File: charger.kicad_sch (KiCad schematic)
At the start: 39 parts, among them Q1 NMOS, Q2 NMOS, Q3 NMOS, SW3 SW_SPST, U2 BQ25798RQMR

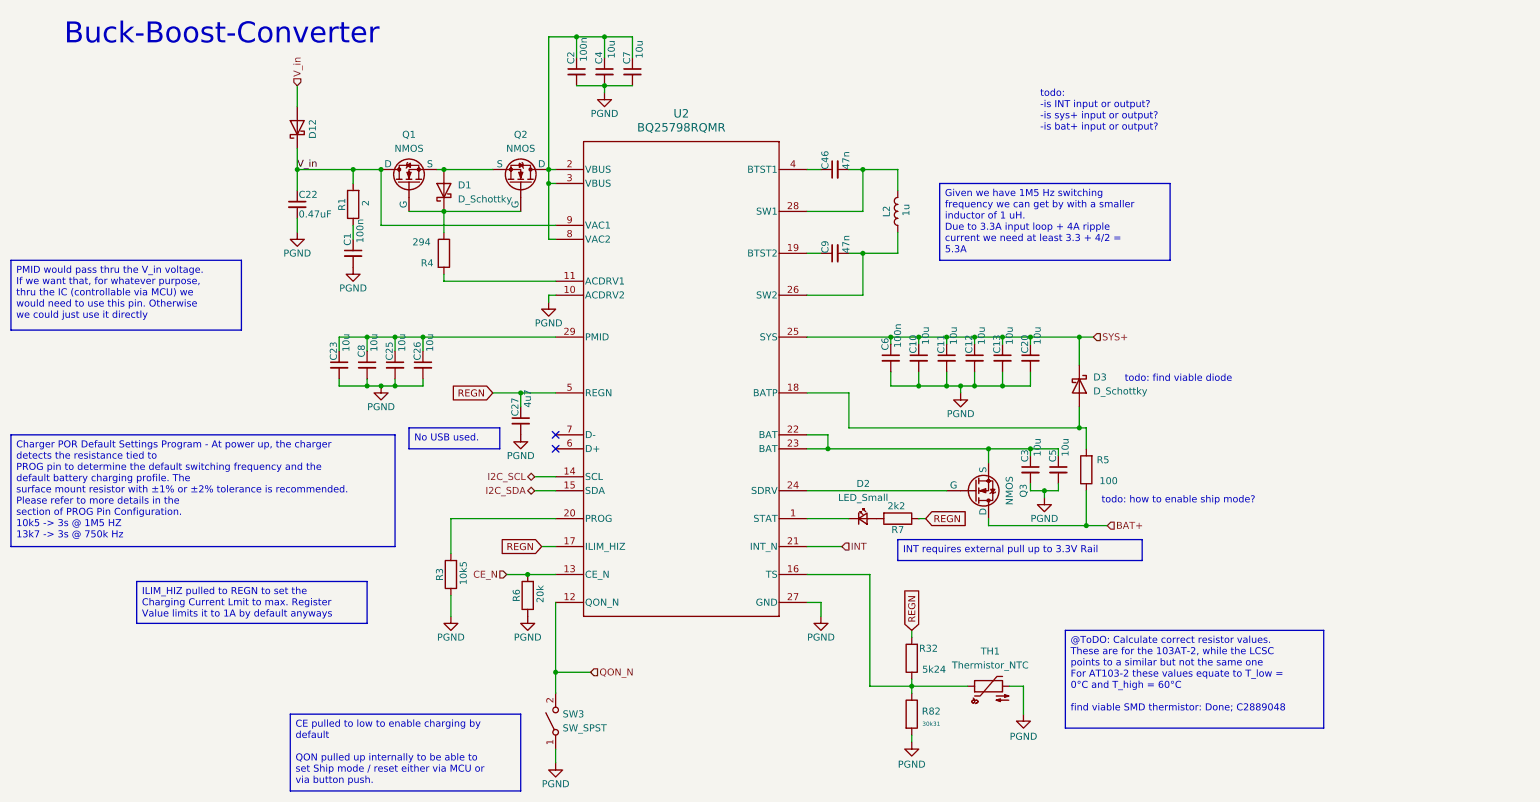
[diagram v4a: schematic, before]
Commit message: cleaned up hierarchical structure; changed connectors
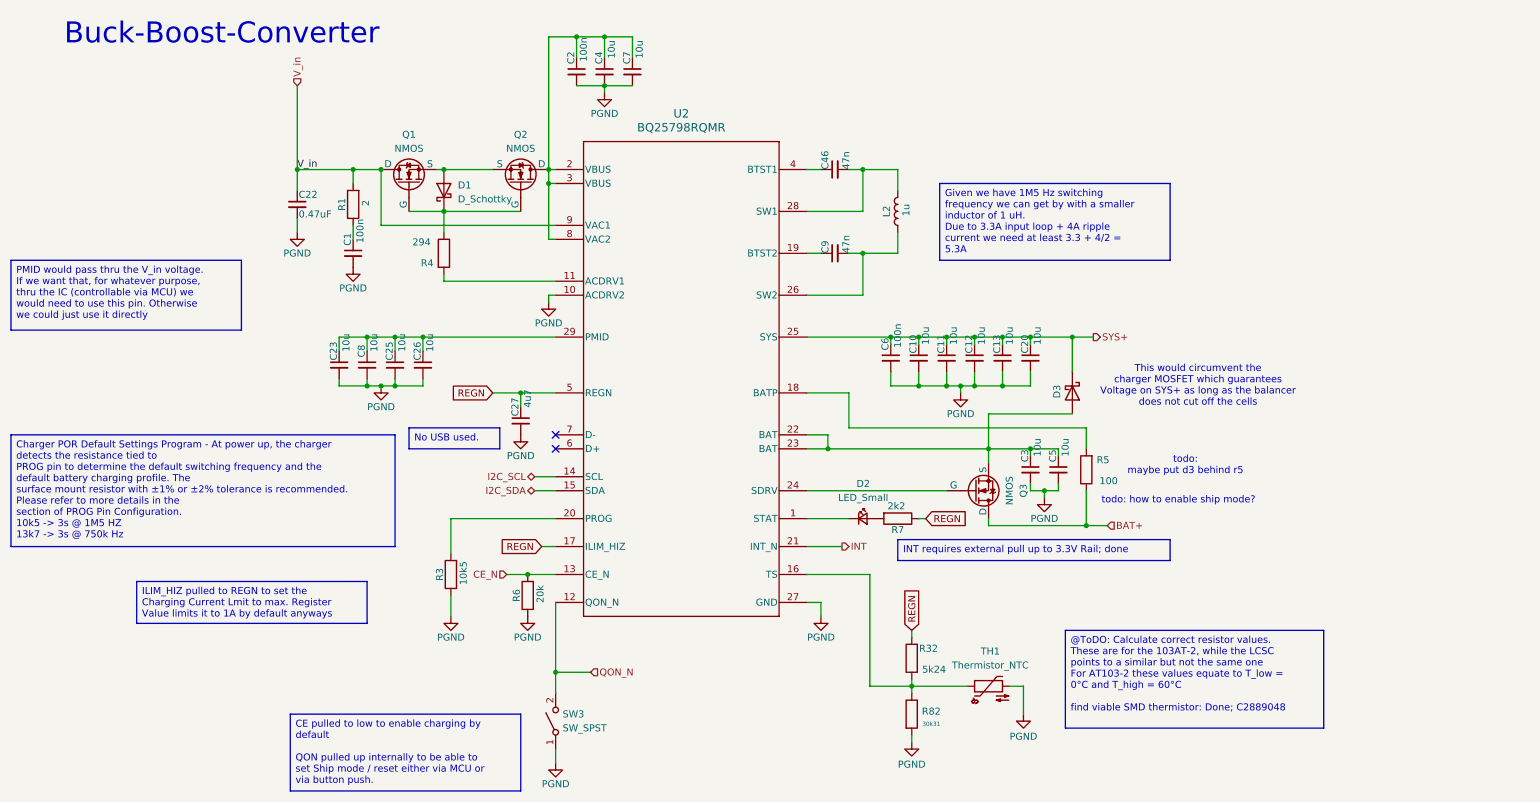
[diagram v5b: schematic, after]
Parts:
- removed D12: ~, Diode_SMD:D_SMA, symbol Device:D_Schottky
- D3: value D_Schottky -> ~; footprint (none) -> Diode_SMD:D_SMA; LCSC (none) -> C3011043
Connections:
- net at R5.2, U2.18 (BATP): no longer D3.2 (A)
- net at C3.1, C5.1, Q3.3 (S)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: now also D3.2 (A)
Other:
- note added: "This would circumvent the charger MOSFET which guarantees Voltage on SYS+ as long as the balancer does not cut off the cells"
- note added: "todo: maybe put d3 behind r5"
- note removed: "todo: -is INT input or output? -is sys+ input or output? -is bat+ input or output?"
- note removed: "todo: find viable diode"
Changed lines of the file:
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@@
 		)
 	)
-	(text "todo: \n-is INT input or output?\n-is sys+ input or output?\n-is bat+ input or output?"
+	(text "todo: \nmaybe put d3 behind r5"
 		(exclude_from_sim no)
-		(at 201.168 31.242 0)
+		(at 227.584 95.758 0)
 		(effects
 			(font
 				(size 1.27 1.27)
 			)
-			(justify left)
 		)
 	)
-	(text "todo: find viable diode"
+	(text "This would circumvent the \ncharger MOSFET which guarantees\nVoltage on SYS+ as long as the balancer \ndoes not cut off the cells"
 		(exclude_from_sim no)
-		(at 226.314 80.01 0)
+		(at 229.87 81.28 0)
 		(effects
 			(font
@@
 		)
 	)
-	(text_box "INT requires external pull up to 3.3V Rail"
+	(text_box "INT requires external pull up to 3.3V Rail; done"
 		(exclude_from_sim no)
 		(at 175.26 109.22 0)
-		(size 44.45 3.81)
+		(size 49.53 3.81)
 		(margins 0.9525 0.9525 0.9525 0.9525)
 		(stroke
@@
 	)
 	(junction
-		(at 208.28 72.39)
-		(diameter 0)
-		(color 0 0 0 0)
-	)
-	(junction
 		(at 111.76 41.91)
 		(diameter 0)
@@
 	)
 	(junction
-		(at 208.28 88.9)
-		(diameter 0)
-		(color 0 0 0 0)
-	)
-	(junction
 		(at 168.91 41.91)
 		(diameter 0)
@@
 	)
 	(junction
+		(at 207.01 72.39)
+		(diameter 0)
+		(color 0 0 0 0)
+	)
+	(junction
 		(at 199.39 72.39)
 		(diameter 0)
@@
 	(wire
 		(pts
-			(xy 208.28 72.39) (xy 208.28 77.47)
-		)
-		(stroke
-			(width 0)
-			(type default)
-		)
-	)
-	(wire
-		(pts
 			(xy 204.47 100.33) (xy 201.93 100.33)
 		)
@@
 	(wire
 		(pts
-			(xy 166.37 88.9) (xy 208.28 88.9)
-		)
-		(stroke
-			(width 0)
-			(type default)
-		)
-	)
-	(wire
-		(pts
 			(xy 66.04 41.91) (xy 66.04 45.72)
 		)
@@
 	(wire
 		(pts
-			(xy 66.04 50.8) (xy 66.04 53.34)
+			(xy 191.77 86.36) (xy 191.77 92.71)
 		)
 		(stroke
@@
 	(wire
 		(pts
-			(xy 158.75 41.91) (xy 161.29 41.91)
+			(xy 66.04 50.8) (xy 66.04 53.34)
 		)
 		(stroke
@@
 	(wire
 		(pts
-			(xy 175.26 57.15) (xy 168.91 57.15)
+			(xy 158.75 41.91) (xy 161.29 41.91)
 		)
 		(stroke
@@
 	(wire
 		(pts
-			(xy 113.03 54.61) (xy 111.76 54.61)
+			(xy 175.26 57.15) (xy 168.91 57.15)
 		)
 		(stroke
@@
 	(wire
 		(pts
-			(xy 66.04 26.67) (xy 66.04 30.48)
+			(xy 113.03 54.61) (xy 111.76 54.61)
 		)
 		(stroke
@@
 	(wire
 		(pts
-			(xy 208.28 88.9) (xy 209.55 88.9)
+			(xy 166.37 88.9) (xy 209.55 88.9)
 		)
 		(stroke
@@
 	(wire
 		(pts
-			(xy 208.28 72.39) (xy 199.39 72.39)
+			(xy 199.39 72.39) (xy 207.01 72.39)
 		)
 		(stroke
@@
 	(wire
 		(pts
+			(xy 207.01 72.39) (xy 207.01 78.74)
+		)
+		(stroke
+			(width 0)
+			(type default)
+		)
+	)
+	(wire
+		(pts
 			(xy 88.9 81.28) (xy 83.82 81.28)
 		)
@@
 	(wire
 		(pts
-			(xy 66.04 38.1) (xy 66.04 41.91)
+			(xy 66.04 26.67) (xy 66.04 41.91)
 		)
 		(stroke
@@
 	(wire
 		(pts
+			(xy 207.01 72.39) (xy 210.82 72.39)
+		)
+		(stroke
+			(width 0)
+			(type default)
+		)
+	)
+	(wire
+		(pts
 			(xy 184.15 73.66) (xy 184.15 72.39)
 		)
@@
 	(wire
 		(pts
+			(xy 191.77 86.36) (xy 207.01 86.36)
+		)
+		(stroke
+			(width 0)
+			(type default)
+		)
+	)
+	(wire
+		(pts
 			(xy 162.56 92.71) (xy 191.77 92.71)
 		)
@@
 	(wire
 		(pts
-			(xy 208.28 85.09) (xy 208.28 88.9)
-		)
-		(stroke
-			(width 0)
-			(type default)
-		)
-	)
-	(wire
-		(pts
 			(xy 168.91 41.91) (xy 175.26 41.91)
 		)
@@
 	(wire
 		(pts
-			(xy 210.82 72.39) (xy 208.28 72.39)
-		)
-		(stroke
-			(width 0)
-			(type default)
-		)
-	)
-	(wire
-		(pts
 			(xy 88.9 80.01) (xy 88.9 81.28)
 		)
@@
 	)
 	(hierarchical_label "INT"
-		(shape input)
+		(shape output)
 		(at 165.1 110.49 0)
 		(effects
@@
 	)
 	(hierarchical_label "SYS+"
-		(shape input)
+		(shape output)
 		(at 210.82 72.39 0)
 		(effects
@@
 	)
 	(symbol
-		(lib_id "Device:D_Schottky")
-		(at 208.28 81.28 270)
-		(unit 1)
-		(exclude_from_sim no)
-		(in_bom yes)
-		(on_board yes)
-		(dnp no)
-		(fields_autoplaced yes)
-		(property "Reference" "D3"
-			(at 210.82 79.6924 90)
-			(effects
-				(font
-					(size 1.27 1.27)
-				)
-				(justify left)
-			)
-		)
-		(property "Value" "D_Schottky"
-			(at 210.82 82.2324 90)
-			(effects
-				(font
-					(size 1.27 1.27)
-				)
-				(justify left)
-			)
-		)
-		(property "Footprint" ""
-			(at 208.28 81.28 0)
-			(effects
-				(font
-					(size 1.27 1.27)
-				)
-				(hide yes)
-			)
-		)
-		(property "Datasheet" "~"
-			(at 208.28 81.28 0)
-			(effects
-				(font
-					(size 1.27 1.27)
-				)
-				(hide yes)
-			)
-		)
-		(property "Description" "Schottky diode"
-			(at 208.28 81.28 0)
-			(effects
-				(font
-					(size 1.27 1.27)
-				)
-				(hide yes)
-			)
-		)
-		(pin "1"
-		)
-		(pin "2"
-		)
-		(instances
-			(project ""
-				(path "/afc8cbd3-9ea8-40a2-afae-ed6bd0fe7e6e/29a18ff5-2f4c-44c0-998a-9c2a7b324824"
-					(reference "D3")
-					(unit 1)
-				)
-			)
-		)
-	)
-	(symbol
 		(lib_id "Device:R")
 		(at 92.71 57.15 0)
@@
 	)
 	(symbol
-		(lib_id "Device:D_Schottky")
-		(at 66.04 34.29 90)
+		(lib_id "power:GND1")
+		(at 201.93 101.6 0)
 		(unit 1)
 		(exclude_from_sim no)
@@
 		(on_board yes)
 		(dnp no)
-		(property "Reference" "D12"
-			(at 68.834 34.544 0)
-			(effects
-				(font
-					(size 1.27 1.27)
-				)
-			)
-		)
-		(property "Value" "~"
-			(at 69.85 34.6075 0)
+		(property "Reference" "#PWR011"
+			(at 201.93 107.95 0)
 			(effects
 				(font
@@
 			)
 		)
-		(property "Footprint" "Diode_SMD:D_SMA"
-			(at 66.04 34.29 0)
+		(property "Value" "PGND"
+			(at 201.93 105.41 0)
 			(effects
 				(font
 					(size 1.27 1.27)
 				)
-				(hide yes)
 			)
 		)
-		(property "Datasheet" "https://www.lcsc.com/datasheet/C22452.pdf"
-			(at 66.04 34.29 0)
+		(property "Footprint" ""
+			(at 201.93 101.6 0)
 			(effects
 				(font
@@
 			)
 		)
-		(property "Description" "Schottky diode"
-			(at 66.04 34.29 0)
+		(property "Datasheet" ""
+			(at 201.93 101.6 0)
 			(effects
 				(font
@@
 			)
 		)
-		(property "LCSC" "C22452"
-			(at 66.04 34.29 0)
+		(property "Description" "Power symbol creates a global label with name \"GND1\" , ground"
+			(at 201.93 101.6 0)
 			(effects
 				(font
@@
 			)
 		)
-		(pin "2"
-		)
 		(pin "1"
 		)
@@
 			(project "rapid_power_module"
 				(path "/afc8cbd3-9ea8-40a2-afae-ed6bd0fe7e6e/29a18ff5-2f4c-44c0-998a-9c2a7b324824"
-					(reference "D12")
+					(reference "#PWR011")
 					(unit 1)
 				)
@@
 	)
 	(symbol
-		(lib_id "power:GND1")
-		(at 201.93 101.6 0)
+		(lib_id "Device:D_Schottky")
+		(at 207.01 82.55 270)
 		(unit 1)
 		(exclude_from_sim no)
@@
 		(on_board yes)
 		(dnp no)
-		(property "Reference" "#PWR011"
-			(at 201.93 107.95 0)
+		(property "Reference" "D3"
+			(at 204.216 82.296 0)
+			(effects
+				(font
+					(size 1.27 1.27)
+				)
+			)
+		)
+		(property "Value" "~"
+			(at 203.2 82.2325 0)
 			(effects
 				(font
@@
 			)
 		)
-		(property "Value" "PGND"
-			(at 201.93 105.41 0)
+		(property "Footprint" "Diode_SMD:D_SMA"
+			(at 207.01 82.55 0)
 			(effects
 				(font
 					(size 1.27 1.27)
 				)
+				(hide yes)
 			)
 		)
-		(property "Footprint" ""
-			(at 201.93 101.6 0)
+		(property "Datasheet" "https://www.lcsc.com/datasheet/C22452.pdf"
+			(at 207.01 82.55 0)
 			(effects
 				(font
@@
 			)
 		)
-		(property "Datasheet" ""
-			(at 201.93 101.6 0)
+		(property "Description" "High Current Diode"
+			(at 207.01 82.55 0)
 			(effects
 				(font
@@
 			)
 		)
-		(property "Description" "Power symbol creates a global label with name \"GND1\" , ground"
-			(at 201.93 101.6 0)
+		(property "LCSC" "C3011043"
+			(at 207.01 82.55 0)
 			(effects
 				(font
@@
 			)
 		)
+		(pin "2"
+		)
 		(pin "1"
 		)
@@
 			(project "rapid_power_module"
 				(path "/afc8cbd3-9ea8-40a2-afae-ed6bd0fe7e6e/29a18ff5-2f4c-44c0-998a-9c2a7b324824"
-					(reference "#PWR011")
+					(reference "D3")
 					(unit 1)
 				)

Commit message: finalized new balancer layout (removed R_SNS and implemented the resulting consequences); removed charger shipping mode
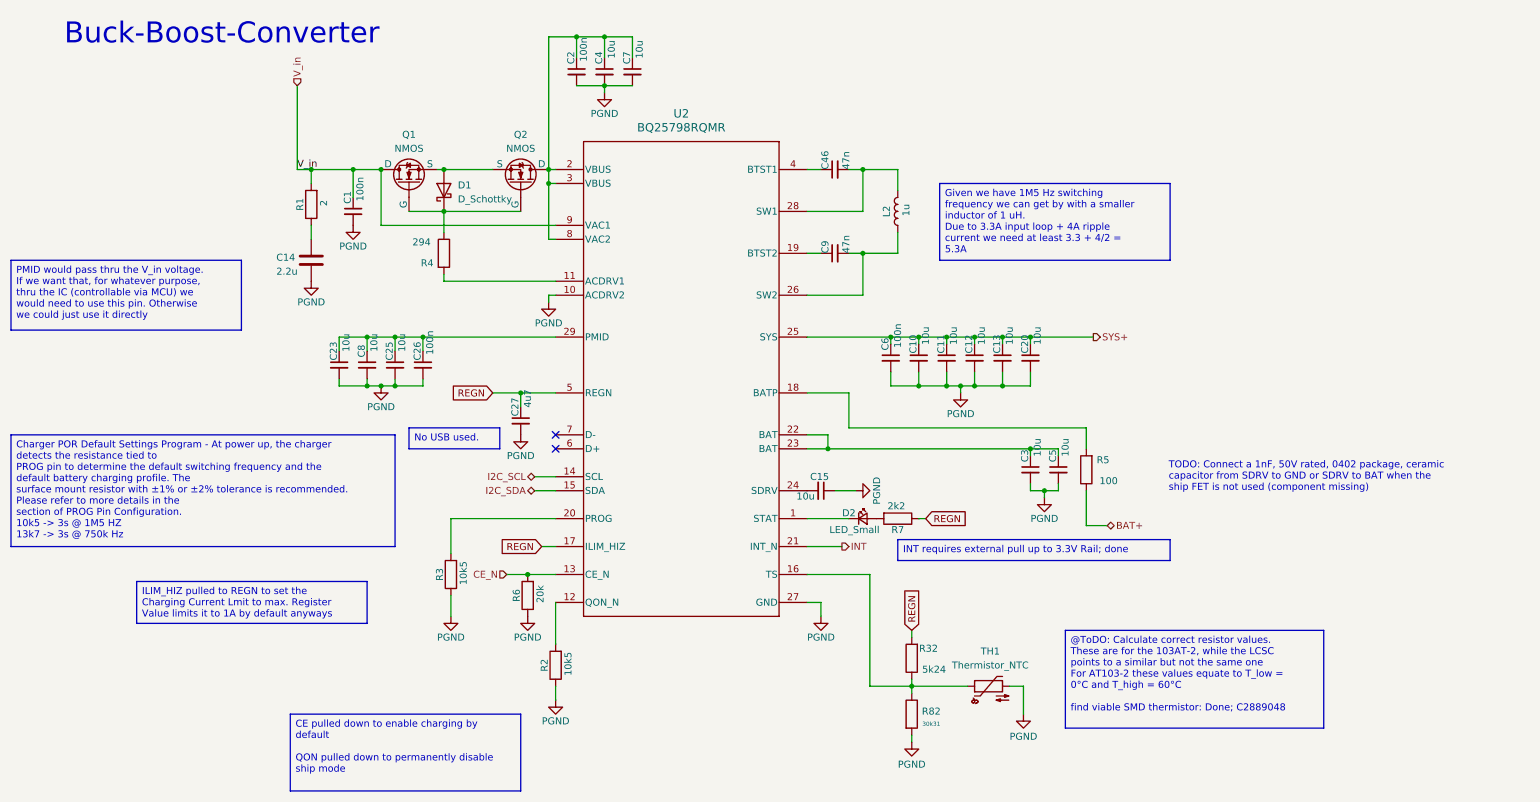
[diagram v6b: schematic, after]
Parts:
- removed C22: 0.47uF, Capacitor_SMD:C_0402_1005Metric, symbol Device:C_Small
- removed D3: ~, Diode_SMD:D_SMA, symbol Device:D_Schottky
- removed Q3: NMOS, symbol Simulation_SPICE:NMOS
- removed SW3: SW_SPST, symbol Switch:SW_SPST
- added C14: 2.2u, symbol Device:C
- added C15: 10u, Capacitor_SMD:C_0402_1005Metric, symbol Device:C_Small
- added R2: 10k5, Resistor_SMD:R_0402_1005Metric, symbol Device:R
- C26: value 10u -> 100n
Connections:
- net PGND: now also C14.2, C15.1, R2.1
- net V_in: now also C1.1
- net at U2.24 (SDRV): now also C15.2
- net at R1.1: now also C14.1; no longer C1.1
- net QON_N: no longer names the net of U2.12 (QON_N)
- net QON_N: now also R2.2
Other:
- note added: "TODO: Connect a 1nF, 50V rated, 0402 package, ceramic capacitor from SDRV to GND or SDRV to BAT when the ship FET is not used (component missing)"
- note removed: "This would circumvent the charger MOSFET which guarantees Voltage on SYS+ as long as the balancer does not cut off the cells"
- note removed: "todo: how to enable ship mode?"
- note removed: "todo: maybe put d3 behind r5"
- moved on the sheet: C1, R1
